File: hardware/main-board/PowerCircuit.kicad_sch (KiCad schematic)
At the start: 38 parts, among them J9 Barrel_Jack, U31 XTPS55285VALR, U32 TPS54202DDC, U33 LM2776

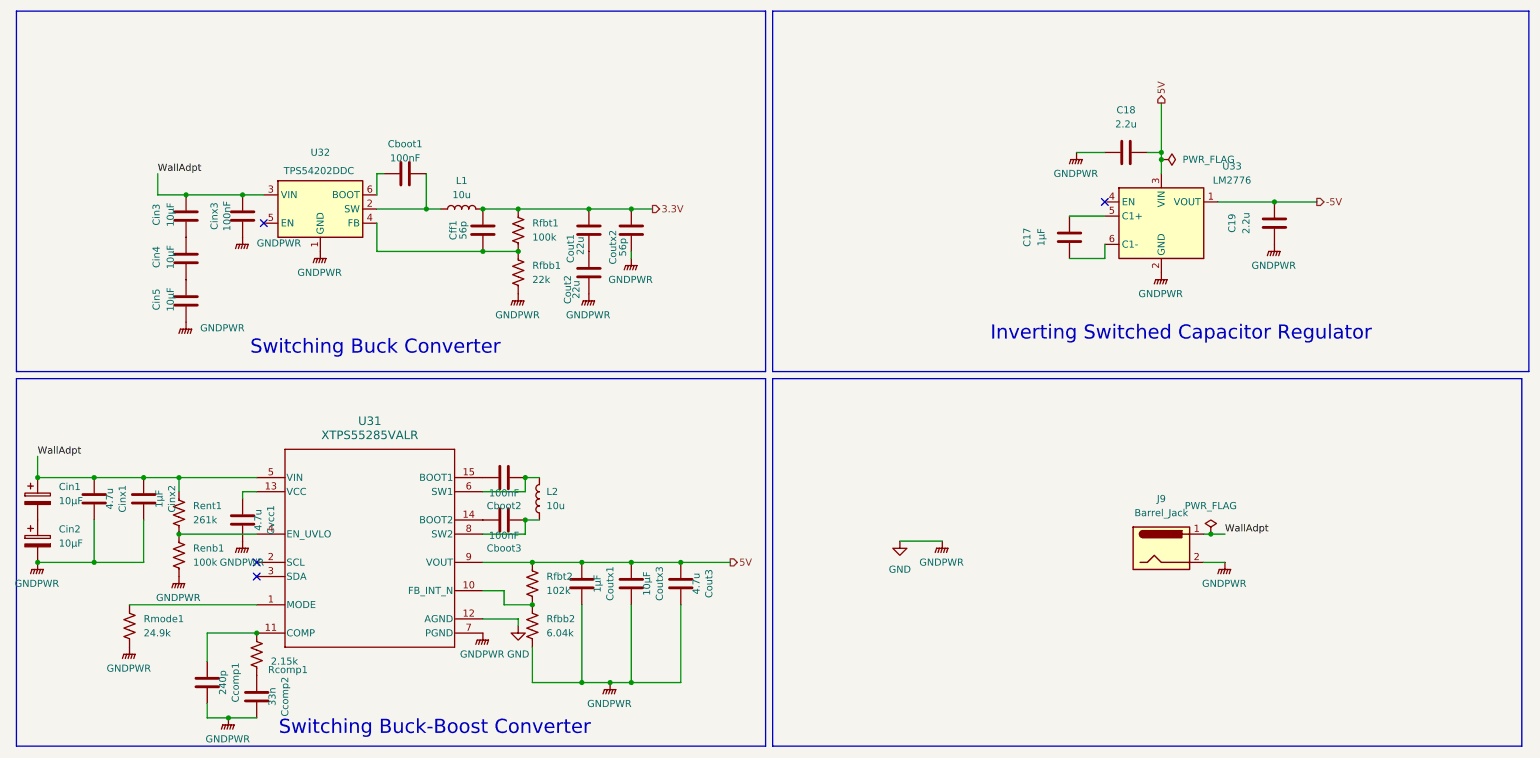
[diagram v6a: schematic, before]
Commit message: finalized component list, fixed DRC errors
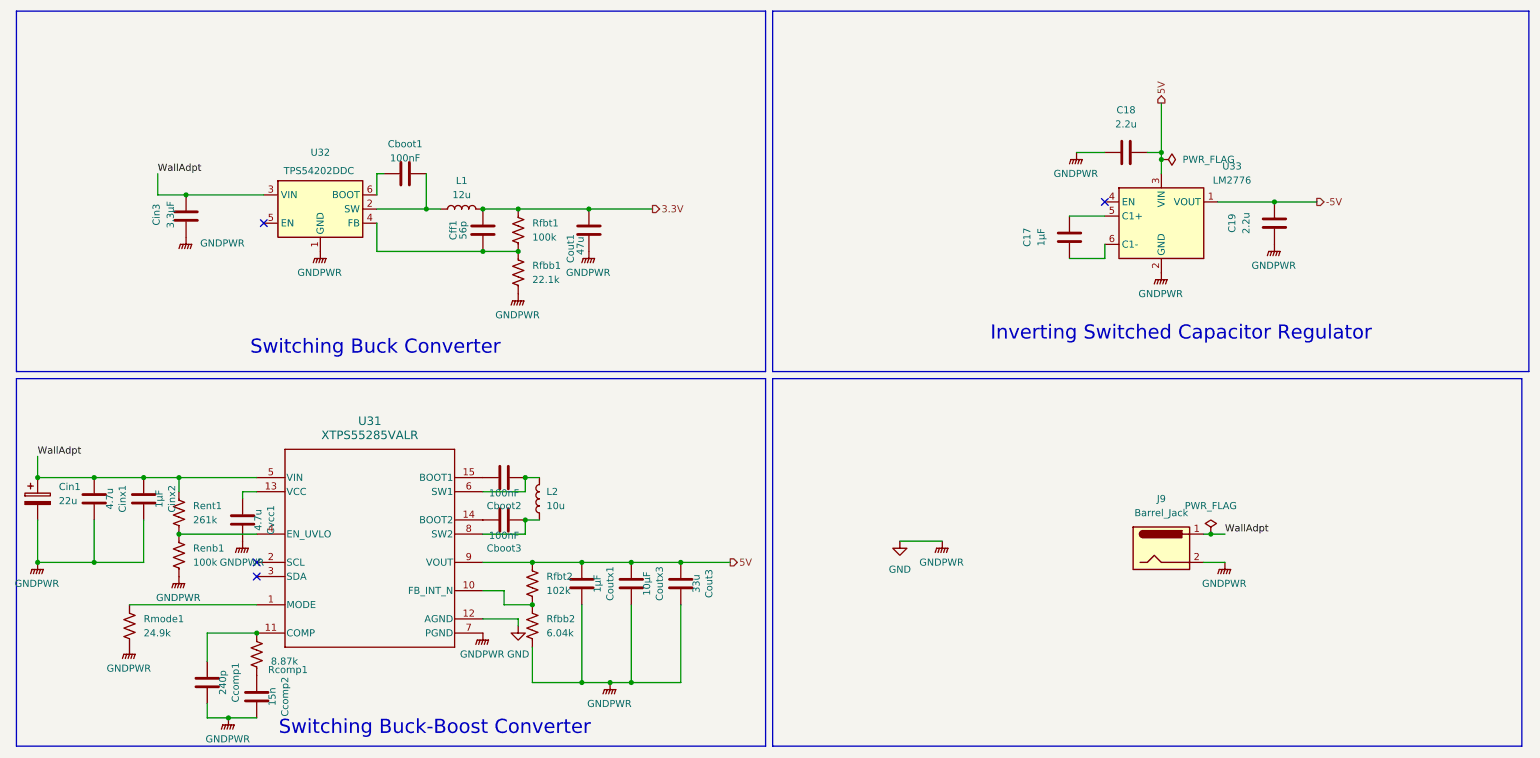
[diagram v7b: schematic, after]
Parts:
- removed Cin2: 10µF, SeniorDesignFP:CAP_EEFK_C_PAN, symbol Device:C_Polarized
- removed Cin4, Cin5: 10µF, Capacitor_SMD:C_1210_3225Metric_Pad1.33x2.70mm_HandSolder, symbol Device:C
- removed Cinx3: 100nF, Capacitor_SMD:C_0402_1005Metric_Pad0.74x0.62mm_HandSolder, symbol Device:C
- removed Cout2: 22u, Capacitor_SMD:C_0805_2012Metric_Pad1.18x1.45mm_HandSolder, symbol Device:C
- removed Coutx2: 56p, Resistor_SMD:R_0402_1005Metric_Pad0.72x0.64mm_HandSolder, symbol Device:C
- C18, C19: DKPN (none) -> CL10B225KP8NNNC
- Cboot1: footprint Capacitor_SMD:C_0402_1005Metric_Pad0.74x0.62mm_HandSolder -> Capacitor_SMD:C_0805_2012Metric_Pad1.18x1.45mm_HandSolder; DKPN (none) -> C0805C104M5RACTU
- Cboot2, Cboot3: DKPN (none) -> GRM155R71C104KA88D
- Ccomp1: DKPN (none) -> GRM1555C1H241JA01D
- Ccomp2: value 33n -> 15n; DKPN (none) -> GRM155R71C153KA01D
- Cff1: DKPN (none) -> GRM0335C1E560JA01D
- Cin1: value 10µF -> 22u; DKPN (none) -> 35SVPF22M
- Cin3: value 10µF -> 3.3µF; DKPN (none) -> C1608X5R1V335K080AC
- Cinx1: DKPN (none) -> MSASU32MSB7475MPNA01
- Cinx2: DKPN (none) -> C1005X5R1V105K050BC
- Cout1: value 22u -> 47u; DKPN (none) -> GRM32ER61C476KE15L
- Cout3: value 4.7u -> 33u; footprint Capacitor_SMD:C_1206_3216Metric_Pad1.33x1.80mm_HandSolder -> Capacitor_Tantalum_SMD:CP_EIA-3528-21_Kemet-B_HandSolder; DKPN (none) -> TPSB336K016R0350
- Coutx1: DKPN (none) -> C0603C105Z8VACTU
- Coutx3: DKPN (none) -> C3225X7R1H106M250AC
- Cvcc1: DKPN (none) -> C1608X5R1C475K080AC
- J9: DKPN (none) -> PJ-063AH
- L1: value 10u -> 12u; footprint Inductor_SMD:L_Bourns-SRU1028_10.0x10.0mm -> SeniorDesignFP:IND_4532-WE-PD2_WRE-L; DKPN (none) -> NPI43C120MTRF
- L2: footprint Inductor_SMD:L_Bourns_SDR0604 -> Inductor_SMD:L_Bourns_SRN6045TA; DKPN (none) -> SRN6045-100M
- Rcomp1: value 2.15k -> 8.87k; DKPN (none) -> CRCW04028K87FKED
- Renb1, Rfbt1: DKPN (none) -> CRCW0402100KFKED
- Rent1: DKPN (none) -> CRCW0402261KFKED
- Rfbb1: value 22k -> 22.1k; footprint Resistor_SMD:R_0201_0603Metric_Pad0.64x0.40mm_HandSolder -> Resistor_SMD:R_0402_1005Metric_Pad0.72x0.64mm_HandSolder; DKPN (none) -> CRCW040222K1FKED
- Rfbb2: DKPN (none) -> CRCW04026K04FKED
- Rfbt2: DKPN (none) -> CRCW0402102KFKED
- Rmode1: DKPN (none) -> CRCW040224K9FKED
- U31: DKPN (none) -> XTPS55285VALR
- U32: DKPN (none) -> TPS54202DDCR
- U33: DKPN (none) -> LM2776DBVR
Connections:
- net GND: now also Cin1.2, Cin3.1, Cout1.1
